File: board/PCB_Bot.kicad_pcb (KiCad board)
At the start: 2 copper layers, 34.5 x 40.1 mm, 18 parts, among them J1 Screw_Terminal_01x04, J2 Conn_02x15_Top_Bottom, J3 Conn_02x15_Top_Bottom, J4 Screw_Terminal_01x02, J5 Screw_Terminal_01x03, U1 TB6612FNG, U2 LSM9DS1

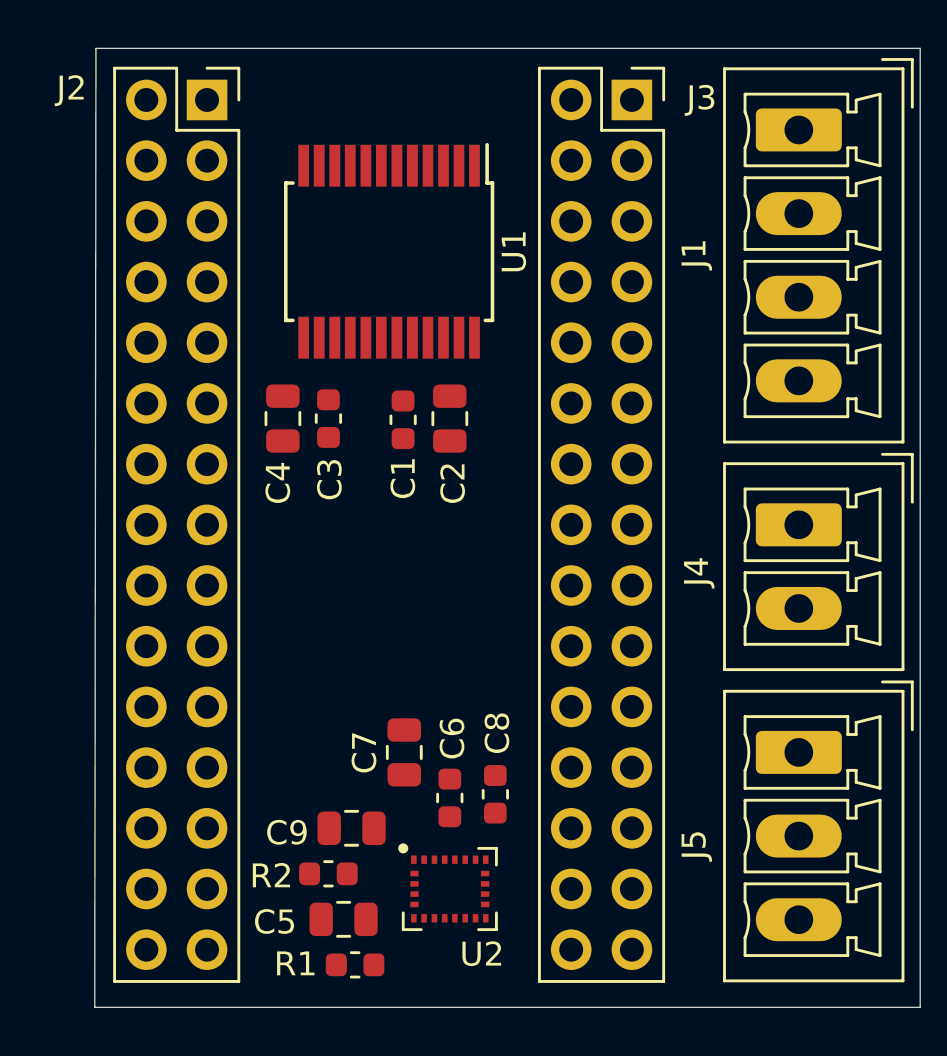
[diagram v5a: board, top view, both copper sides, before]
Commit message: update pcbnew, add new track widths
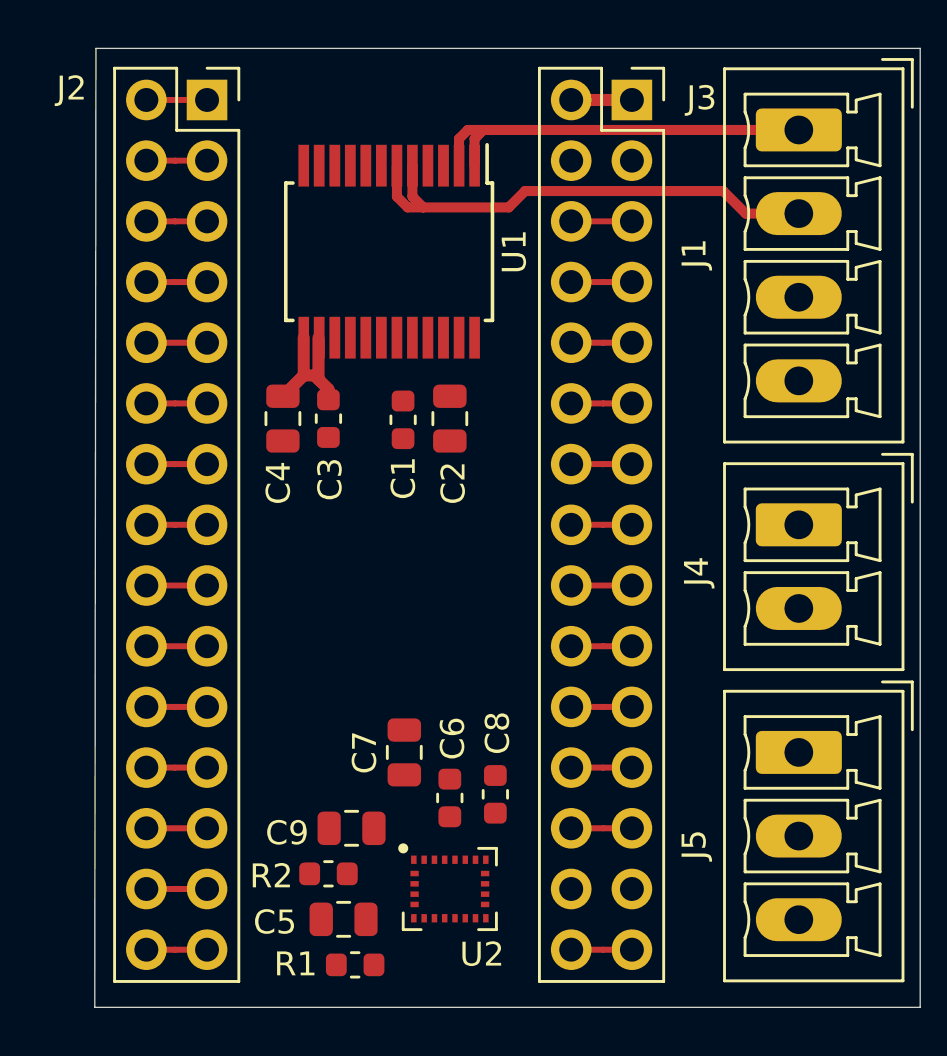
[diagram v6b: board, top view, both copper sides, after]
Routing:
- net Net-(J1-Pad2): track 0.00 -> 20.9 mm
- net Net-(J1-Pad1): track 0.00 -> 17.1 mm
- net VIN: track 0.00 -> 8.81 mm
- net TX1: track 0.00 -> 2.54 mm
- net RX0: track 0.00 -> 2.54 mm
- net RST1: track 0.00 -> 2.54 mm
- net RST: track 0.00 -> 2.54 mm
- net REF: track 0.00 -> 2.54 mm
- net GND: track 0.00 -> 2.54 mm
- net D9: track 0.00 -> 2.54 mm
- net D8: track 0.00 -> 2.54 mm
- net D7: track 0.00 -> 2.54 mm
- net D6: track 0.00 -> 2.54 mm
- net D5: track 0.00 -> 2.54 mm
- net D4: track 0.00 -> 2.54 mm
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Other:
- net class Default_Clr added: clearance 0.1524, trace_width 0.25, via_dia 0.8, via_drill 0.4
- net class MTR_PWR added: clearance 0.2, trace_width 0.42, via_dia 0.8, via_drill 0.4
- net class Power added: clearance 0.2, trace_width 0.508, via_dia 0.8, via_drill 0.4
- net class Small added: clearance 0.1524, trace_width 0.2, via_dia 0.8, via_drill 0.4
- rule trace_min: 0.2 -> 0.1524
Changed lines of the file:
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@@
     (thickness 1.6)
     (drawings 4)
-    (tracks 0)
+    (tracks 71)
     (zones 0)
     (modules 18)
@@
   (setup
     (last_trace_width 0.25)
+    (user_trace_width 0.508)
     (trace_clearance 0.2)
     (zone_clearance 0.508)
     (zone_45_only no)
-    (trace_min 0.2)
+    (trace_min 0.1524)
     (via_size 0.8)
     (via_drill 0.4)
@@
     (add_net "Net-(C8-Pad1)")
     (add_net "Net-(C9-Pad1)")
-    (add_net "Net-(J1-Pad1)")
-    (add_net "Net-(J1-Pad2)")
-    (add_net "Net-(J1-Pad3)")
-    (add_net "Net-(J1-Pad4)")
     (add_net "Net-(U2-Pad10)")
     (add_net "Net-(U2-Pad11)")
@@
     (add_net RX0)
     (add_net TX1)
+  )
+  (net_class Default_Clr ""
+    (clearance 0.1524)
+    (trace_width 0.25)
+    (via_dia 0.8)
+    (via_drill 0.4)
+    (uvia_dia 0.3)
+    (uvia_drill 0.1)
+  )
+  (net_class MTR_PWR ""
+    (clearance 0.2)
+    (trace_width 0.42)
+    (via_dia 0.8)
+    (via_drill 0.4)
+    (uvia_dia 0.3)
+    (uvia_drill 0.1)
+    (add_net "Net-(J1-Pad1)")
+    (add_net "Net-(J1-Pad2)")
+    (add_net "Net-(J1-Pad3)")
+    (add_net "Net-(J1-Pad4)")
+  )
+  (net_class Power ""
+    (clearance 0.2)
+    (trace_width 0.508)
+    (via_dia 0.8)
+    (via_drill 0.4)
+    (uvia_dia 0.3)
+    (uvia_drill 0.1)
     (add_net VIN)
+  )
+  (net_class Small ""
+    (clearance 0.1524)
+    (trace_width 0.2)
+    (via_dia 0.8)
+    (via_drill 0.4)
+    (uvia_dia 0.3)
+    (uvia_drill 0.1)
   )
   (module Package_LGA:LGA-24L_3x3.5mm_P0.43mm (layer F.Cu)
@@
   (gr_line (start 86.741 110.363) (end 86.7918 70.231) (layer Edge.Cuts) (width 0.05))
   (gr_line (start 121.285 110.363) (end 86.741 110.363) (layer Edge.Cuts) (width 0.05))
+  (segment (start 90.102081 80.01) (end 91.44 80.01) (width 0.25) (layer F.Cu) (net 6))
+  (segment (start 88.9 80.01) (end 90.102081 80.01) (width 0.25) (layer F.Cu) (net 6))
+  (segment (start 108.017919 80.01) (end 106.68 80.01) (width 0.25) (layer F.Cu) (net 7))
+  (segment (start 109.22 80.01) (end 108.017919 80.01) (width 0.25) (layer F.Cu) (net 7))
+  (segment (start 96.105999 84.085999) (end 96.105999 82.34) (width 0.508) (layer F.Cu) (net 8))
+  (segment (start 96.52 84.9375) (end 96.52 84.5) (width 0.508) (layer F.Cu) (net 8))
+  (segment (start 96.52 84.5) (end 96.105999 84.085999) (width 0.508) (layer F.Cu) (net 8))
+  (segment (start 95.485 83.9175) (end 95.485 82.34) (width 0.508) (layer F.Cu) (net 8))
+  (segment (start 94.615 84.7875) (end 95.485 83.9175) (width 0.508) (layer F.Cu) (net 8))
+  (segment (start 95.9375 83.9175) (end 96.105999 84.085999) (width 0.508) (layer F.Cu) (net 8))
+  (segment (start 95.485 83.9175) (end 95.9375 83.9175) (width 0.508) (layer F.Cu) (net 8))
+  (segment (start 106.68 72.39) (end 109.22 72.39) (width 0.508) (layer F.Cu) (net 8))
+  (segment (start 102.635 74.015) (end 102.635 75.14) (width 0.42) (layer F.Cu) (net 12))
+  (segment (start 103.005 73.645) (end 102.635 74.015) (width 0.42) (layer F.Cu) (net 12))
+  (segment (start 116.205 73.645) (end 103.005 73.645) (width 0.42) (layer F.Cu) (net 12))
+  (segment (start 101.985 74.015) (end 101.985 75.14) (width 0.42) (layer F.Cu) (net 12))
+  (segment (start 102.355 73.645) (end 101.985 74.015) (width 0.42) (layer F.Cu) (net 12))
+  (segment (start 103.005 73.645) (end 102.355 73.645) (width 0.42) (layer F.Cu) (net 12))
+  (segment (start 100.035 76.435) (end 100.035 75.14) (width 0.42) (layer F.Cu) (net 13))
+  (segment (start 116.205 77.145) (end 113.985 77.145) (width 0.42) (layer F.Cu) (net 13))
+  (segment (start 104.7496 76.2) (end 104.0638 76.8858) (width 0.42) (layer F.Cu) (net 13))
+  (segment (start 100.4858 76.8858) (end 100.035 76.435) (width 0.42) (layer F.Cu) (net 13))
+  (segment (start 113.985 77.145) (end 113.04 76.2) (width 0.42) (layer F.Cu) (net 13))
+  (segment (start 113.04 76.2) (end 104.7496 76.2) (width 0.42) (layer F.Cu) (net 13))
+  (segment (start 104.0638 76.8858) (end 100.4858 76.8858) (width 0.42) (layer F.Cu) (net 13))
+  (segment (start 99.385 76.435) (end 99.385 75.14) (width 0.42) (layer F.Cu) (net 13))
+  (segment (start 99.8358 76.8858) (end 99.385 76.435) (width 0.42) (layer F.Cu) (net 13))
+  (segment (start 100.4858 76.8858) (end 99.8358 76.8858) (width 0.42) (layer F.Cu) (net 13))
+  (segment (start 88.9 72.39) (end 91.44 72.39) (width 0.25) (layer F.Cu) (net 16))
+  (segment (start 90.102081 74.93) (end 91.44 74.93) (width 0.25) (layer F.Cu) (net 17))
+  (segment (start 88.9 74.93) (end 90.102081 74.93) (width 0.25) (layer F.Cu) (net 17))
+  (segment (start 90.102081 77.47) (end 91.44 77.47) (width 0.25) (layer F.Cu) (net 18))
+  (segment (start 88.9 77.47) (end 90.102081 77.47) (width 0.25) (layer F.Cu) (net 18))
+  (segment (start 91.44 82.55) (end 88.9 82.55) (width 0.25) (layer F.Cu) (net 19))
+  (segment (start 90.102081 85.09) (end 91.44 85.09) (width 0.25) (layer F.Cu) (net 20))
+  (segment (start 88.9 85.09) (end 90.102081 85.09) (width 0.25) (layer F.Cu) (net 20))
+  (segment (start 90.102081 87.63) (end 91.44 87.63) (width 0.25) (layer F.Cu) (net 21))
+  (segment (start 88.9 87.63) (end 90.102081 87.63) (width 0.25) (layer F.Cu) (net 21))
+  (segment (start 90.102081 90.17) (end 91.44 90.17) (width 0.25) (layer F.Cu) (net 22))
+  (segment (start 88.9 90.17) (end 90.102081 90.17) (width 0.25) (layer F.Cu) (net 22))
+  (segment (start 88.9 92.71) (end 91.44 92.71) (width 0.25) (layer F.Cu) (net 23))
+  (segment (start 88.9 95.25) (end 91.44 95.25) (width 0.25) (layer F.Cu) (net 24))
+  (segment (start 90.102081 97.79) (end 91.44 97.79) (width 0.25) (layer F.Cu) (net 25))
+  (segment (start 88.9 97.79) (end 90.102081 97.79) (width 0.25) (layer F.Cu) (net 25))
+  (segment (start 90.102081 100.33) (end 91.44 100.33) (width 0.25) (layer F.Cu) (net 26))
+  (segment (start 88.9 100.33) (end 90.102081 100.33) (width 0.25) (layer F.Cu) (net 26))
+  (segment (start 88.9 102.87) (end 91.44 102.87) (width 0.25) (layer F.Cu) (net 27))
+  (segment (start 90.237919 105.41) (end 88.9 105.41) (width 0.25) (layer F.Cu) (net 28))
+  (segment (start 91.44 105.41) (end 90.237919 105.41) (width 0.25) (layer F.Cu) (net 28))
+  (segment (start 90.102081 107.95) (end 91.44 107.95) (width 0.25) (layer F.Cu) (net 29))
+  (segment (start 88.9 107.95) (end 90.102081 107.95) (width 0.25) (layer F.Cu) (net 29))
+  (segment (start 108.017919 82.55) (end 106.68 82.55) (width 0.25) (layer F.Cu) (net 30))
+  (segment (start 109.22 82.55) (end 108.017919 82.55) (width 0.25) (layer F.Cu) (net 30))
+  (segment (start 108.017919 85.09) (end 106.68 85.09) (width 0.25) (layer F.Cu) (net 31))
+  (segment (start 109.22 85.09) (end 108.017919 85.09) (width 0.25) (layer F.Cu) (net 31))
+  (segment (start 108.017919 87.63) (end 106.68 87.63) (width 0.25) (layer F.Cu) (net 32))
+  (segment (start 109.22 87.63) (end 108.017919 87.63) (width 0.25) (layer F.Cu) (net 32))
+  (segment (start 108.017919 90.17) (end 106.68 90.17) (width 0.25) (layer F.Cu) (net 33))
+  (segment (start 109.22 90.17) (end 108.017919 90.17) (width 0.25) (layer F.Cu) (net 33))
+  (segment (start 109.22 92.71) (end 106.68 92.71) (width 0.25) (layer F.Cu) (net 34))
+  (segment (start 108.017919 95.25) (end 106.68 95.25) (width 0.25) (layer F.Cu) (net 35))
+  (segment (start 109.22 95.25) (end 108.017919 95.25) (width 0.25) (layer F.Cu) (net 35))
+  (segment (start 108.017919 97.79) (end 106.68 97.79) (width 0.25) (layer F.Cu) (net 36))
+  (segment (start 109.22 97.79) (end 108.017919 97.79) (width 0.25) (layer F.Cu) (net 36))
+  (segment (start 108.017919 100.33) (end 106.68 100.33) (width 0.25) (layer F.Cu) (net 37))
+  (segment (start 109.22 100.33) (end 108.017919 100.33) (width 0.25) (layer F.Cu) (net 37))
+  (segment (start 108.017919 102.87) (end 106.68 102.87) (width 0.25) (layer F.Cu) (net 38))
+  (segment (start 109.22 102.87) (end 108.017919 102.87) (width 0.25) (layer F.Cu) (net 38))
+  (segment (start 108.017919 107.95) (end 106.68 107.95) (width 0.25) (layer F.Cu) (net 39))
+  (segment (start 109.22 107.95) (end 108.017919 107.95) (width 0.25) (layer F.Cu) (net 39))
+  (segment (start 109.22 77.47) (end 106.68 77.47) (width 0.25) (layer F.Cu) (net 40))
 )

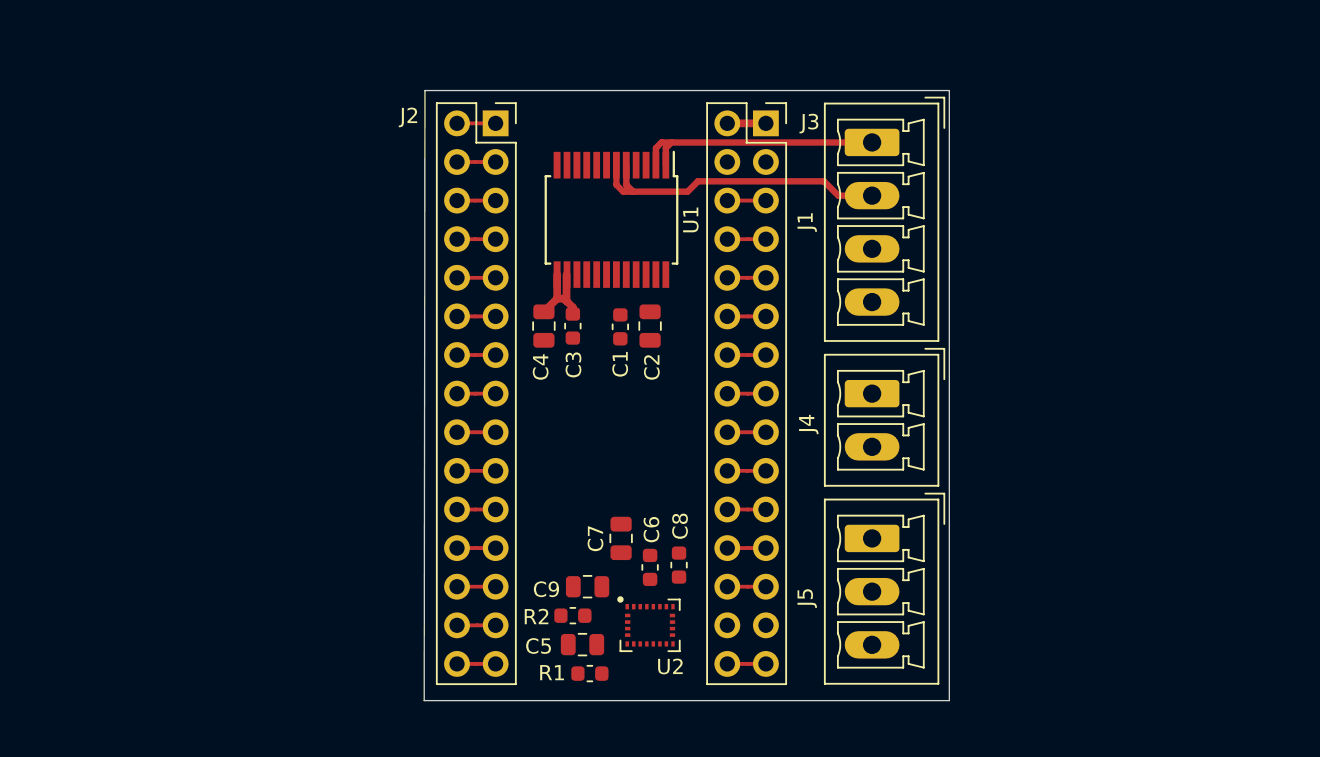
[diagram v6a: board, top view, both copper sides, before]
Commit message: update pcbnew and add some tracks - that can be replaced at some point...
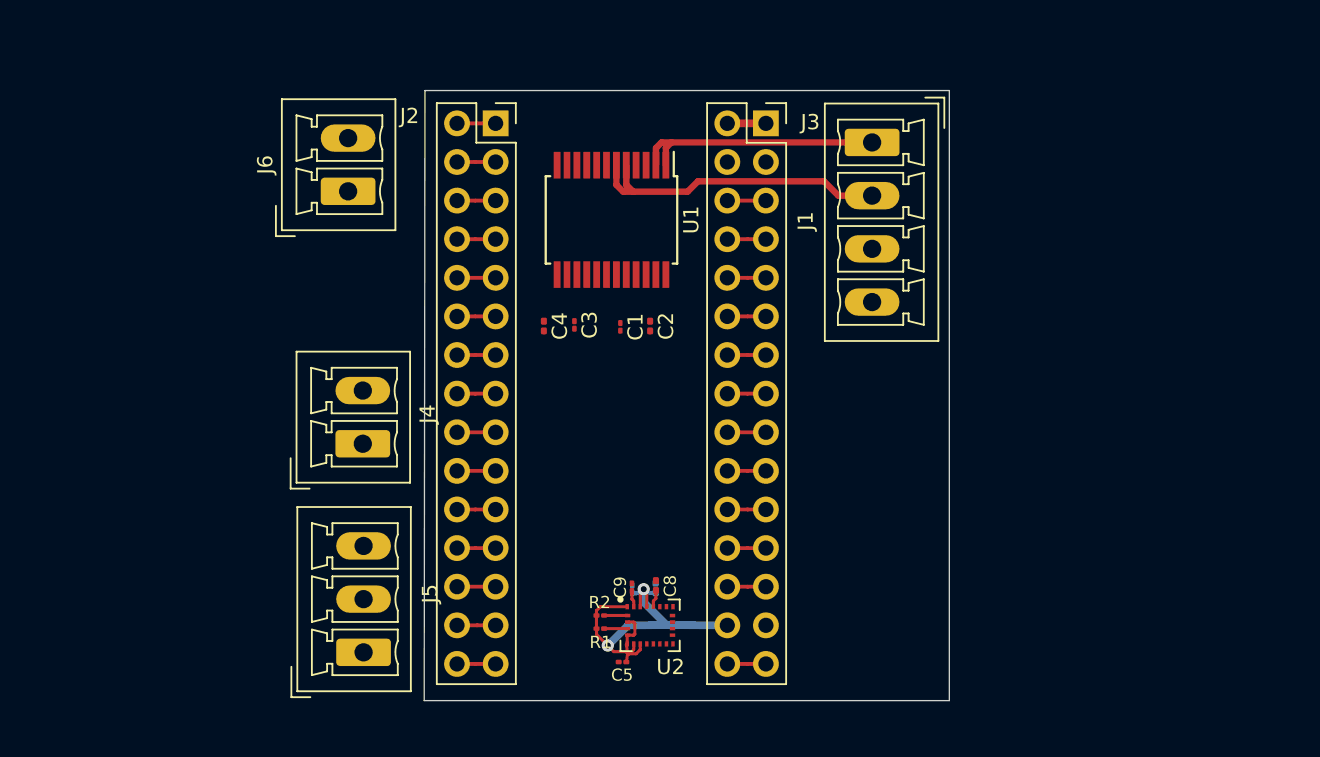
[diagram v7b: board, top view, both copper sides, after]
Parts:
- added J6: Screw_Terminal_01x02, Connector_Phoenix_MC:PhoenixContact_MCV_1,5_2-G-3.5_1x02_P3.50mm_Vertical, F.Cu at (81.7, 76.9)
- C1, C3: footprint Capacitor_SMD:C_0603_1608Metric -> Capacitor_SMD:C_01005_0402Metric
- C2, C4: footprint Capacitor_SMD:C_0805_2012Metric -> Capacitor_SMD:C_0201_0603Metric
- C5, C9: footprint Capacitor_SMD:C_0805_2012Metric -> Capacitor_SMD:C_01005_0402Metric
- C6: footprint Capacitor_SMD:C_0603_1608Metric -> Capacitor_SMD:C_0201_0603Metric; moved to B.Cu
- C7: footprint Capacitor_SMD:C_0805_2012Metric -> Capacitor_SMD:C_01005_0402Metric; moved to B.Cu
- C8: footprint Capacitor_SMD:C_0603_1608Metric -> Capacitor_SMD:C_0201_0603Metric
- R1, R2: footprint Resistor_SMD:R_0603_1608Metric -> Resistor_SMD:R_01005_0402Metric
- moved J5 34.3 mm to (82.8, 107.2), turned to 90 degrees
- moved J4 33.7 mm to (82.7, 93.5), turned to 90 degrees
- moved C7 3.42 mm to (100.4, 103.0)
- moved R1 3.04 mm to (98.3, 105.6)
- moved C9 2.92 mm to (100.4, 102.9), turned to 90 degrees
- moved C5 2.87 mm to (99.8, 107.8)
- moved C8 2.03 mm to (102.0, 102.8)
- moved R2 1.80 mm to (98.3, 104.8)
- moved C6 1.40 mm to (102.0, 103.0)
- moved C3 0.13 mm to (96.6, 85.6)
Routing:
- net 3V3: track 0.00 -> 27.1 mm, vias 0 -> 2
- net VIN: track 8.81 -> 2.54 mm
- net A5: track 2.54 -> 4.09 mm
- net A4: track 2.54 -> 4.09 mm
- net Net-(C8-Pad1): track 0.00 -> 1.15 mm
- net Net-(C9-Pad1): track 0.00 -> 1.08 mm

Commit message: look at layout of nano, add notes_examples to md files
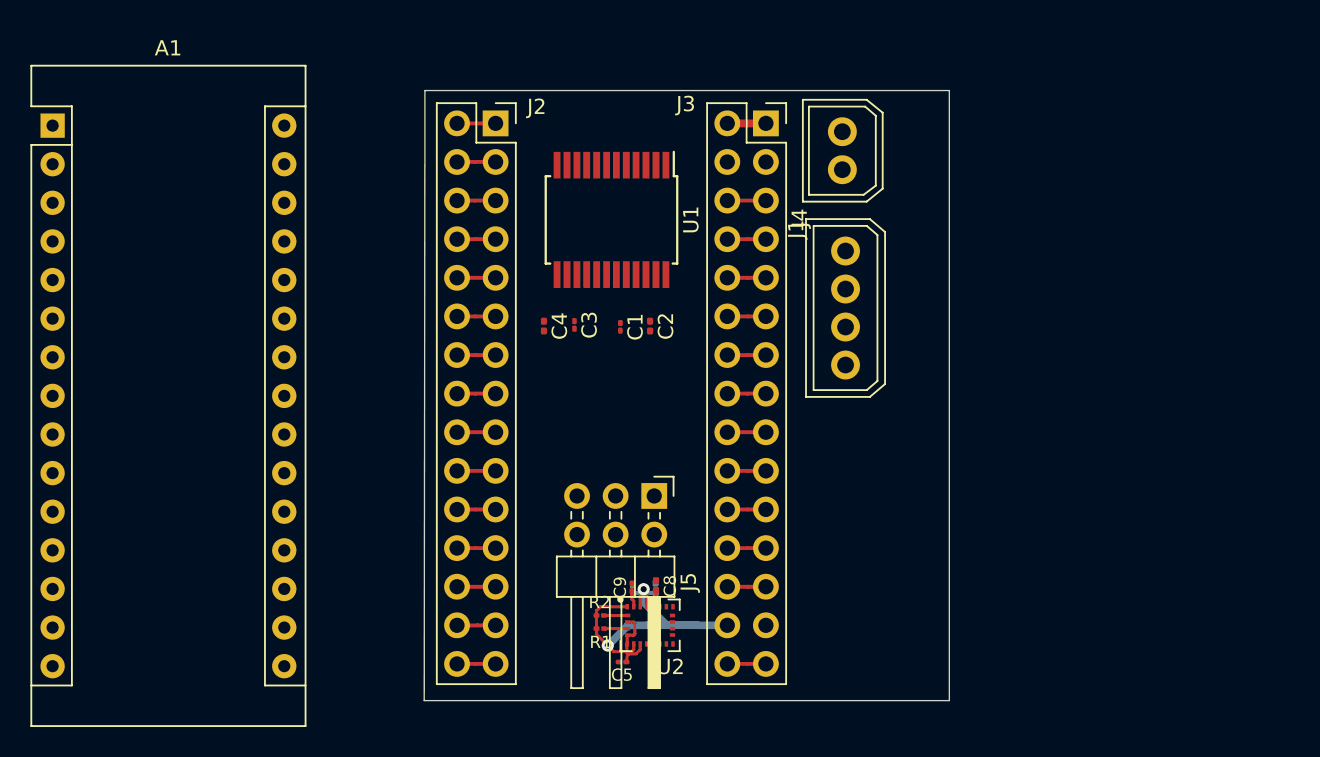
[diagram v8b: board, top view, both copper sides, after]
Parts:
- removed J6: Screw_Terminal_01x02, Connector_Phoenix_MC:PhoenixContact_MCV_1,5_2-G-3.5_1x02_P3.50mm_Vertical
- added A1: Arduino_Nano_v3.x, Module:Arduino_Nano, F.Cu at (62.3, 72.5)
- J1: footprint Connector_Phoenix_MC:PhoenixContact_MCV_1,5_4-G-3.5_1x04_P3.50mm_Vertical -> Rnanobot:PTSM_Phoenix_Contact_4-pos_Base_Strip_1815280
- J4: footprint Connector_Phoenix_MC:PhoenixContact_MCV_1,5_2-G-3.5_1x02_P3.50mm_Vertical -> Rnanobot:PTSM_Phoenix_Contact_2-pos_Base_Strip_1815264
- J5: value Screw_Terminal_01x03 -> Conn_02x03_Top_Bottom; footprint Connector_Phoenix_MC:PhoenixContact_MCV_1,5_3-G-3.5_1x03_P3.50mm_Vertical -> Connector_PinHeader_2.54mm:PinHeader_2x03_P2.54mm_Horizontal
- moved J4 37.0 mm to (114.2, 74.2)
- moved J5 21.7 mm to (101.9, 96.9), turned to 270 degrees
- moved J1 11.0 mm to (114.5, 84.5), turned to 90 degrees
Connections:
- J5 pad 1: D10 -> D12
- J5 pad 2: D11 -> 5V
- J5 pad 3: D12 -> D11
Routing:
- net Net-(J1-Pad2): track 20.9 -> 0.00 mm
- net Net-(J1-Pad1): track 17.1 -> 0.00 mm
